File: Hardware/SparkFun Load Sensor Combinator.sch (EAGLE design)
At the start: 14 parts

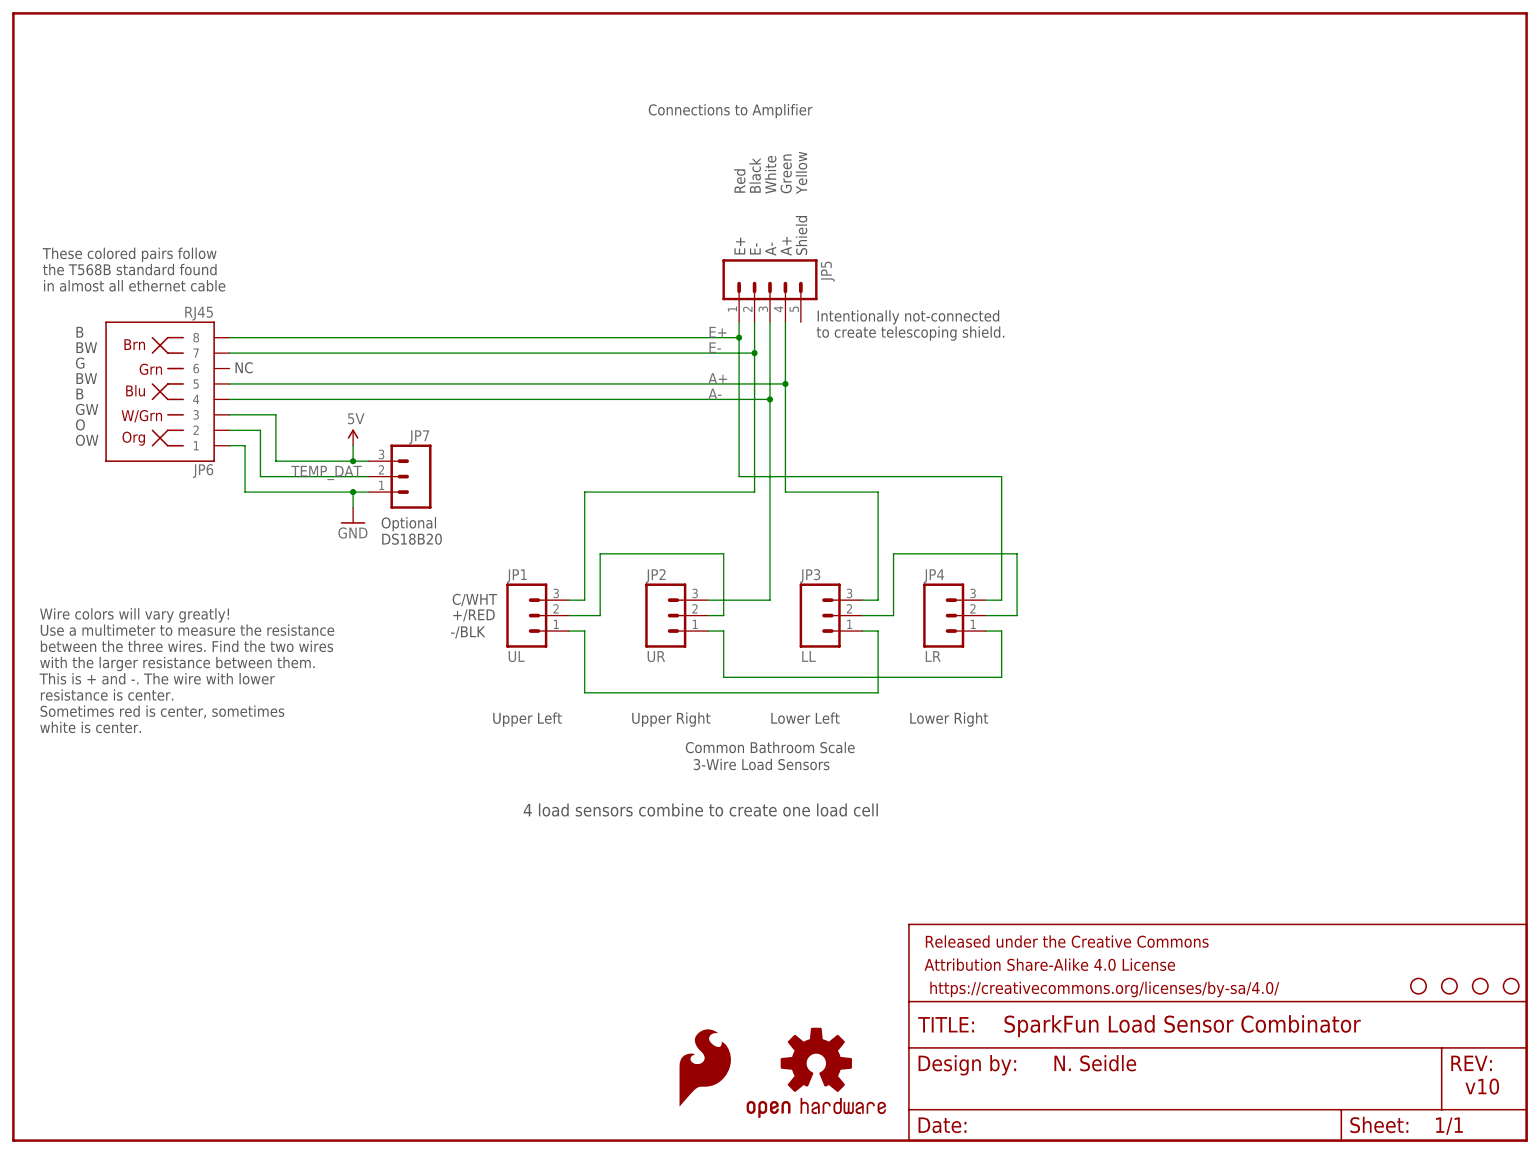
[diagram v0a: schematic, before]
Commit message: Reverting Eagle files back to what is being sold on store front
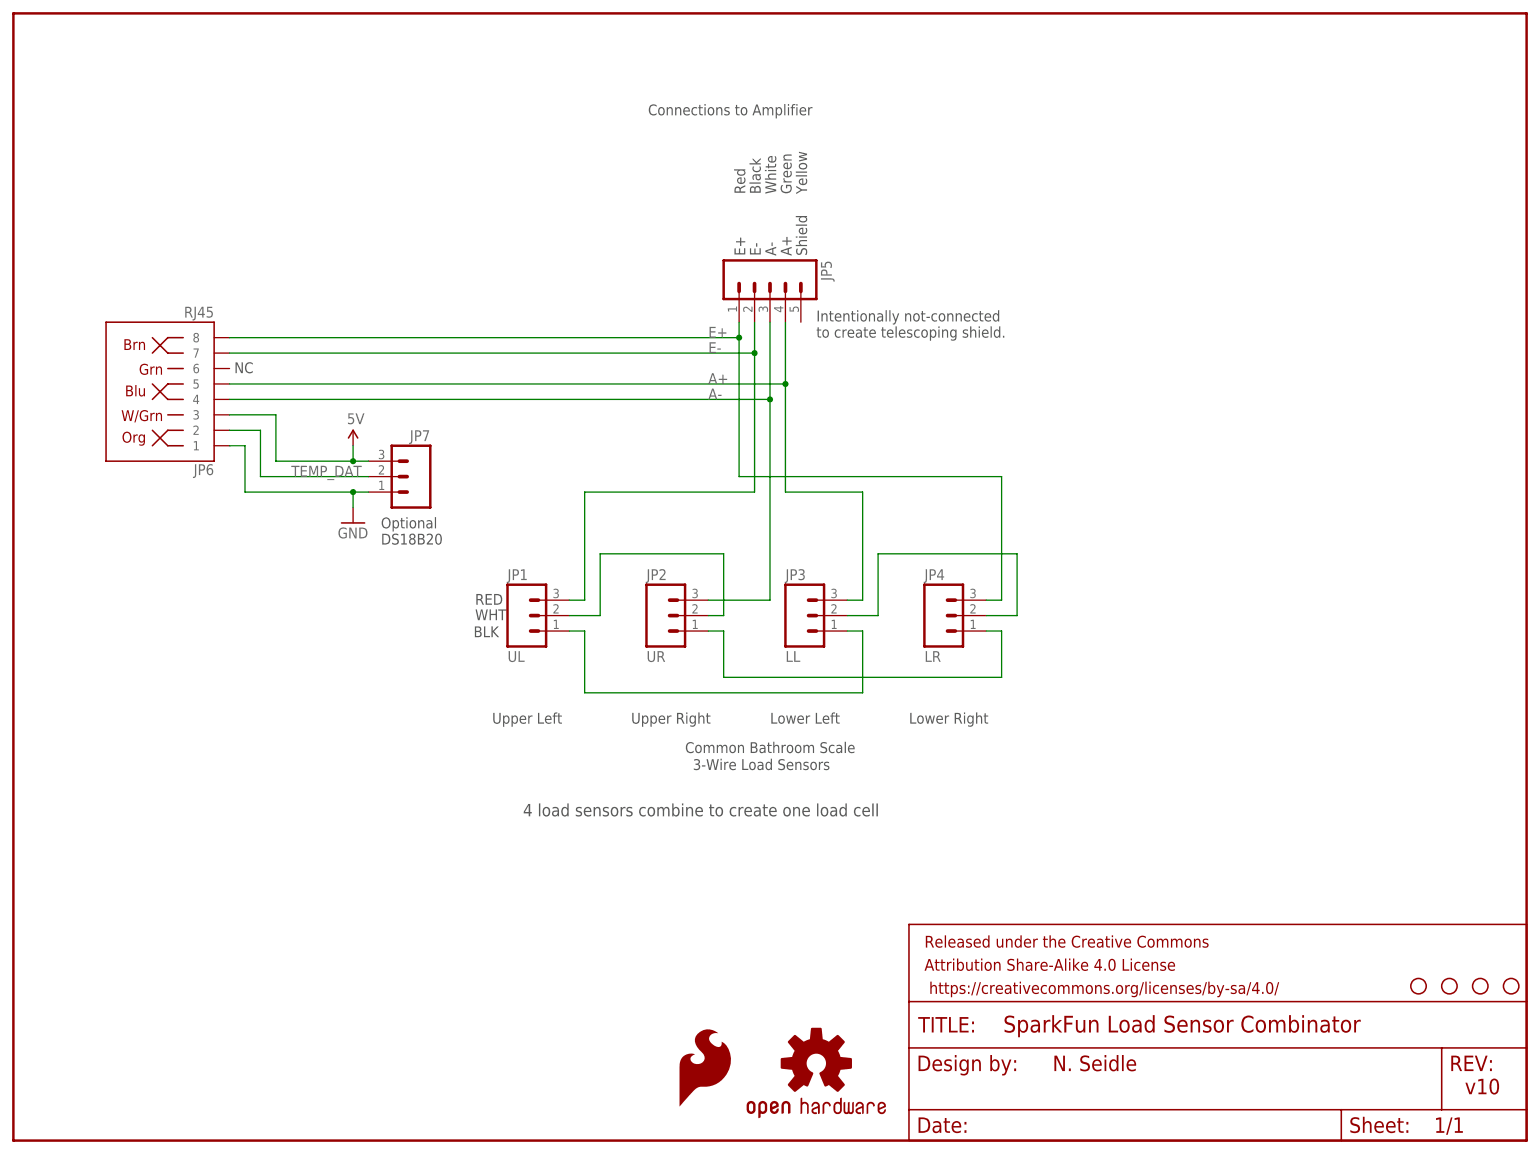
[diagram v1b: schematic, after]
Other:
- note added: "BLK"
- note added: "RED"
- note added: "WHT"
- note removed: "+/RED"
- note removed: "-/BLK"
- note removed: "B"
- note removed: "BW"
- note removed: "C/WHT"
- note removed: "G"
- note removed: "GW"
- note removed: "O"
- note removed: "OW"
- note removed: "These colored pairs follow the T568B standard found in almost all ethernet cable"
- note removed: "Wire colors will vary greatly\! Use a multimeter to measure the resistance between the three wires. Find the two wires with the larger resistance between them. This is + and -. The wire with lower resistance is center. Sometimes red is center, sometimes white is center."
- moved on the sheet: JP3
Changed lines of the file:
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@@
 <text x="120.396" y="155.702" size="1.778" layer="97" rot="R90">Red</text>
 <text x="122.936" y="155.702" size="1.778" layer="97" rot="R90">Black</text>
+<text x="125.476" y="155.702" size="1.778" layer="97" rot="R90">White</text>
+<text x="128.016" y="155.702" size="1.778" layer="97" rot="R90">Green</text>
 <text x="147.32" y="68.58" size="1.778" layer="97">Lower Right</text>
 <text x="101.6" y="68.58" size="1.778" layer="97">Upper Right</text>
@@
 <text x="110.49" y="63.754" size="1.778" layer="97">Common Bathroom Scale</text>
 <text x="104.394" y="168.656" size="1.778" layer="97">Connections to Amplifier</text>
-<text x="71.882" y="82.804" size="1.778" layer="97">-/BLK</text>
-<text x="72.136" y="88.138" size="1.778" layer="97">C/WHT</text>
-<text x="72.136" y="85.598" size="1.778" layer="97">+/RED</text>
+<text x="75.692" y="82.804" size="1.778" layer="97">BLK</text>
+<text x="75.946" y="85.598" size="1.778" layer="97">WHT</text>
+<text x="75.946" y="88.138" size="1.778" layer="97">RED</text>
 <text x="83.82" y="53.34" size="2.032" layer="97">4 load sensors combine to create one load cell</text>
 <text x="130.556" y="145.542" size="1.778" layer="97" rot="R90">Shield</text>
@@
 <text x="170.942" y="11.43" size="2.54" layer="94">N. Seidle</text>
 <text x="238.76" y="7.62" size="2.54" layer="94">v10</text>
-<text x="125.476" y="155.702" size="1.778" layer="97" rot="R90">White</text>
-<text x="128.016" y="155.702" size="1.778" layer="97" rot="R90">Green</text>
-<text x="4.318" y="67.056" size="1.778" layer="97">Wire colors will vary greatly\!
-Use a multimeter to measure the resistance
-between the three wires. Find the two wires
-with the larger resistance between them.
-This is + and -. The wire with lower
-resistance is center.
-Sometimes red is center, sometimes
-white is center.</text>
-<text x="4.826" y="139.7" size="1.778" layer="97">These colored pairs follow
-the T568B standard found
-in almost all ethernet cable</text>
-<text x="10.16" y="129.54" size="1.778" layer="97">BW</text>
-<text x="10.16" y="132.08" size="1.778" layer="97">B</text>
-<text x="10.16" y="127" size="1.778" layer="97">G</text>
-<text x="10.16" y="121.92" size="1.778" layer="97">B</text>
-<text x="10.16" y="124.46" size="1.778" layer="97">BW</text>
-<text x="10.16" y="119.38" size="1.778" layer="97">GW</text>
-<text x="10.16" y="116.84" size="1.778" layer="97">O</text>
-<text x="10.16" y="114.3" size="1.778" layer="97">OW</text>
 </plain>
 <instances>
@@
 <instance part="JP1" gate="G$1" x="83.82" y="86.36"/>
 <instance part="JP2" gate="G$1" x="106.68" y="86.36"/>
-<instance part="JP3" gate="G$1" x="132.08" y="86.36"/>
+<instance part="JP3" gate="G$1" x="129.54" y="86.36"/>
 <instance part="JP4" gate="G$1" x="152.4" y="86.36"/>
 <instance part="FRAME1" gate="G$1" x="0" y="0">
@@
 </instance>
 <instance part="FRAME1" gate="V" x="147.32" y="0"/>
-<instance part="JP5" gate="G$1" x="124.46" y="142.24" smashed="yes" rot="R270">
-<attribute name="VALUE" x="114.3" y="144.78" size="1.778" layer="96" rot="R270"/>
-<attribute name="NAME" x="132.842" y="144.78" size="1.778" layer="95" rot="R270"/>
-</instance>
+<instance part="JP5" gate="G$1" x="124.46" y="142.24" rot="R270"/>
 <instance part="JP6" gate="JP1" x="27.94" y="121.92" rot="R180"/>
 <instance part="JP7" gate="G$1" x="66.04" y="109.22" rot="MR0"/>
@@
 <segment>
 <pinref part="JP3" gate="G$1" pin="1"/>
-<wire x1="139.7" y1="83.82" x2="142.24" y2="83.82" width="0.1524" layer="91"/>
-<wire x1="142.24" y1="83.82" x2="142.24" y2="73.66" width="0.1524" layer="91"/>
-<wire x1="142.24" y1="73.66" x2="93.98" y2="73.66" width="0.1524" layer="91"/>
+<wire x1="137.16" y1="83.82" x2="139.7" y2="83.82" width="0.1524" layer="91"/>
+<wire x1="139.7" y1="83.82" x2="139.7" y2="73.66" width="0.1524" layer="91"/>
+<wire x1="139.7" y1="73.66" x2="93.98" y2="73.66" width="0.1524" layer="91"/>
 <wire x1="93.98" y1="73.66" x2="93.98" y2="83.82" width="0.1524" layer="91"/>
 <pinref part="JP1" gate="G$1" pin="1"/>
@@
 <wire x1="160.02" y1="86.36" x2="165.1" y2="86.36" width="0.1524" layer="91"/>
 <wire x1="165.1" y1="86.36" x2="165.1" y2="96.52" width="0.1524" layer="91"/>
-<wire x1="165.1" y1="96.52" x2="144.78" y2="96.52" width="0.1524" layer="91"/>
-<wire x1="144.78" y1="96.52" x2="144.78" y2="86.36" width="0.1524" layer="91"/>
+<wire x1="165.1" y1="96.52" x2="142.24" y2="96.52" width="0.1524" layer="91"/>
+<wire x1="142.24" y1="96.52" x2="142.24" y2="86.36" width="0.1524" layer="91"/>
 <pinref part="JP3" gate="G$1" pin="2"/>
-<wire x1="144.78" y1="86.36" x2="139.7" y2="86.36" width="0.1524" layer="91"/>
+<wire x1="142.24" y1="86.36" x2="137.16" y2="86.36" width="0.1524" layer="91"/>
 </segment>
 </net>
@@
 <net name="A+" class="0">
 <segment>
-<wire x1="127" y1="106.68" x2="142.24" y2="106.68" width="0.1524" layer="91"/>
-<wire x1="142.24" y1="106.68" x2="142.24" y2="88.9" width="0.1524" layer="91"/>
+<wire x1="127" y1="106.68" x2="139.7" y2="106.68" width="0.1524" layer="91"/>
+<wire x1="139.7" y1="106.68" x2="139.7" y2="88.9" width="0.1524" layer="91"/>
 <pinref part="JP3" gate="G$1" pin="3"/>
-<wire x1="142.24" y1="88.9" x2="139.7" y2="88.9" width="0.1524" layer="91"/>
+<wire x1="139.7" y1="88.9" x2="137.16" y2="88.9" width="0.1524" layer="91"/>
 <wire x1="127" y1="106.68" x2="127" y2="124.46" width="0.1524" layer="91"/>
 <wire x1="127" y1="124.46" x2="35.56" y2="124.46" width="0.1524" layer="91"/>

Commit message: Revision 11 changes
Updated labels from R/W/B to +/-/C and moved temp sensor pins down away
from standoff.
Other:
- note added: "+/WHT"
- note added: "-/BLK"
- note added: "A. Wende"
- note added: "C/RED"
- note added: "Revised by:"
- note added: "Wire colors will vary greatly\! Use a multimeter to measure the resistance between the three wires. Find the two wires with the larger resistance between them. This is + and -. The wire with lower resistance is center. Sometimes red is center, sometimes white is center."
- note added: "v11"
- note removed: "BLK"
- note removed: "RED"
- note removed: "WHT"
- note removed: "v10"
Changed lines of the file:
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@@
 <?xml version="1.0" encoding="utf-8"?>
 <!DOCTYPE eagle SYSTEM "eagle.dtd">
-<eagle version="7.2.0">
+<eagle version="7.5.0">
 <drawing>
 <settings>
@@
 <text x="110.49" y="63.754" size="1.778" layer="97">Common Bathroom Scale</text>
 <text x="104.394" y="168.656" size="1.778" layer="97">Connections to Amplifier</text>
-<text x="75.692" y="82.804" size="1.778" layer="97">BLK</text>
-<text x="75.946" y="85.598" size="1.778" layer="97">WHT</text>
-<text x="75.946" y="88.138" size="1.778" layer="97">RED</text>
+<text x="72.644" y="82.804" size="1.778" layer="97">-/BLK</text>
+<text x="72.644" y="85.598" size="1.778" layer="97">+/WHT</text>
+<text x="72.644" y="88.392" size="1.778" layer="97">C/RED</text>
 <text x="83.82" y="53.34" size="2.032" layer="97">4 load sensors combine to create one load cell</text>
 <text x="130.556" y="145.542" size="1.778" layer="97" rot="R90">Shield</text>
@@
 DS18B20</text>
 <text x="170.942" y="11.43" size="2.54" layer="94">N. Seidle</text>
-<text x="238.76" y="7.62" size="2.54" layer="94">v10</text>
+<text x="238.76" y="7.62" size="2.54" layer="94">v11</text>
+<text x="148.844" y="7.112" size="2.54" layer="94">Revised by:</text>
+<text x="170.942" y="7.112" size="2.54" layer="94">A. Wende</text>
+<text x="10.16" y="73.66" size="1.778" layer="97">Wire colors will vary greatly\!
+Use a multimeter to measure the resistance
+between the three wires. Find the two wires
+with the larger resistance between them.
+This is + and -. The wire with lower
+resistance is center.
+Sometimes red is center, sometimes
+white is center.</text>
 </plain>
 <instances>
